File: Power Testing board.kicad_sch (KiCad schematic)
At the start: 13 parts, among them J1 Conn_01x26_Pin, J2 Conn_01x26_Pin, J3 Conn_01x26_Pin, J4 Conn_01x26_Pin, U1 INA260, U2 INA260, U3 INA260, U4 INA260, U5 TPS26631RGE, U6 TPS26631RGE, U7 TPS26631RGE, U8 TPS26631RGE

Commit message: gnd
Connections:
- net GND: now also U1.11 (GND), U1.6 (GND), U2.11 (GND), U2.6 (GND), U3.11 (GND), U3.6 (GND), U4.11 (GND), U4.6 (GND), U5.25 (GND), U5.8 (GND), U6.25 (GND), U6.8 (GND), U7.25 (GND), U7.8 (GND), U8.25 (GND), U8.8 (GND)
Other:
- moved on the sheet: J1, J2, J3, J4

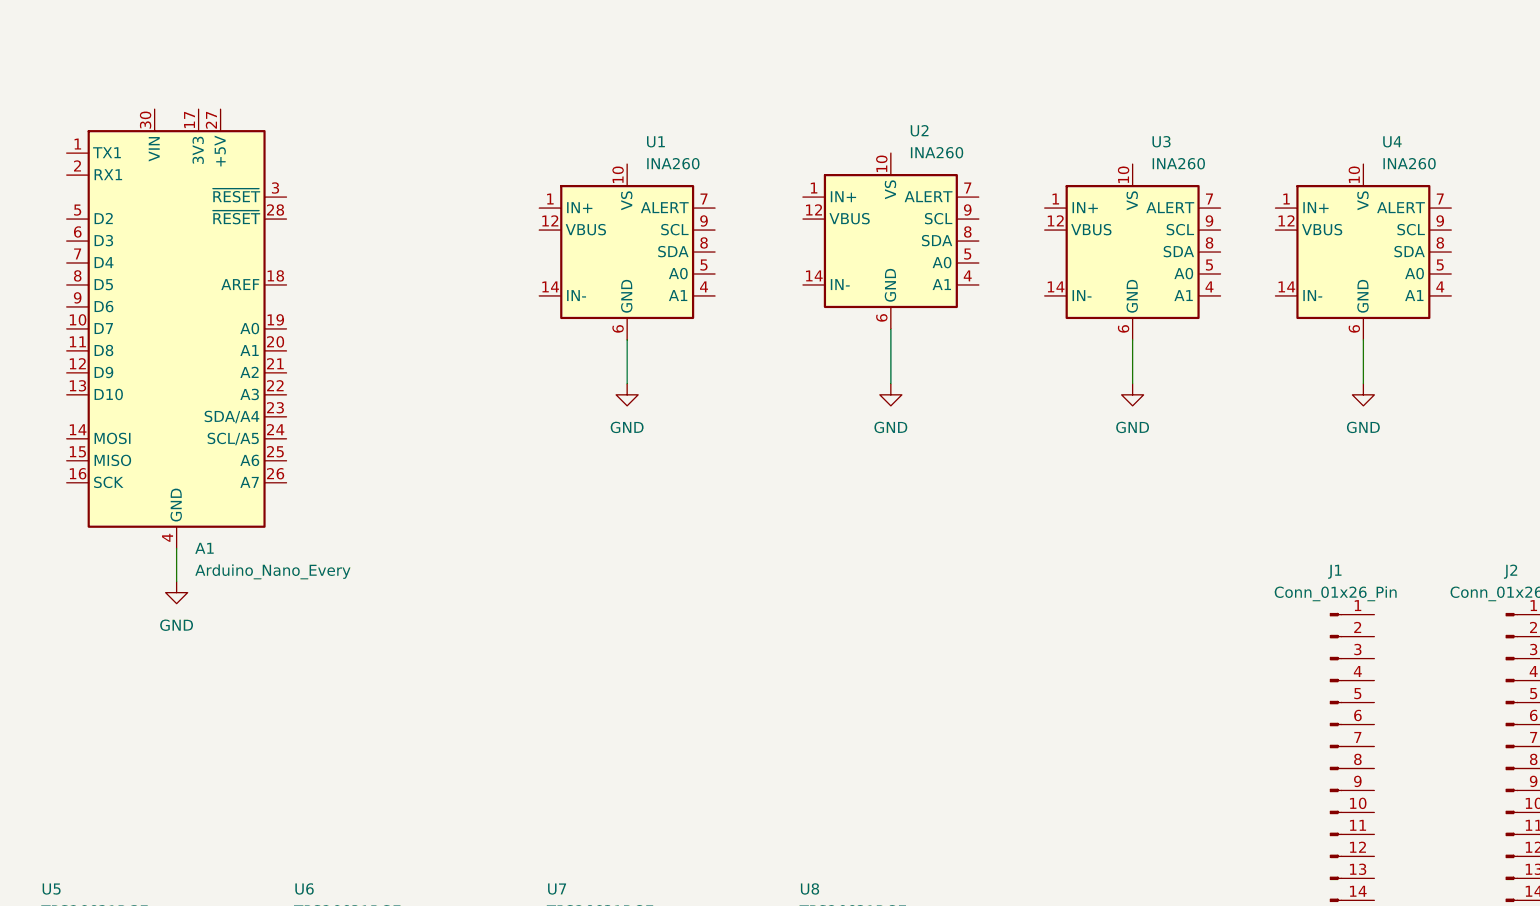
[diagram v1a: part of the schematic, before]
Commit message: ina260 starting connects
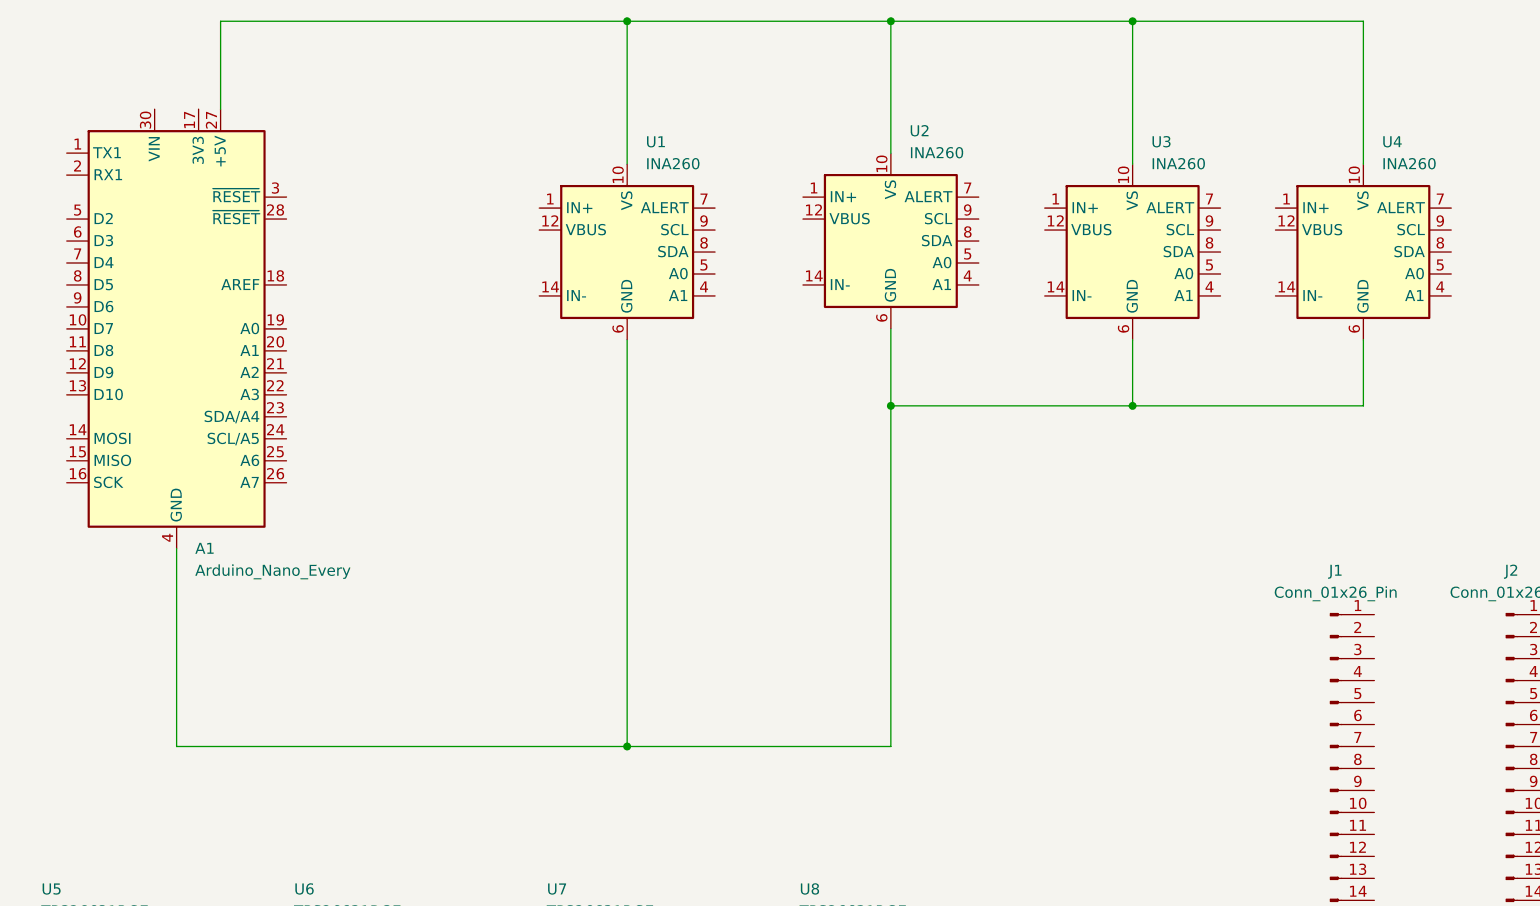
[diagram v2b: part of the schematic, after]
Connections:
- net GND: no longer A1.29 (GND), A1.4 (GND), U1.11 (GND), U1.6 (GND), U2.11 (GND), U2.6 (GND), U3.11 (GND), U3.6 (GND), U4.11 (GND), U4.6 (GND)
- net at U1.10 (VS): now also A1.27 (+5V), U2.10 (VS), U3.10 (VS), U4.10 (VS)
- new net: A1.29 (GND), A1.4 (GND), U1.11 (GND), U1.6 (GND), U2.11 (GND), U2.6 (GND), U3.11 (GND), U3.6 (GND), U4.11 (GND), U4.6 (GND)

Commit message: GN
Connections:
- net GND: now also A1.29 (GND), A1.4 (GND), U1.11 (GND), U1.6 (GND), U2.11 (GND), U2.6 (GND), U3.11 (GND), U3.6 (GND), U4.11 (GND), U4.6 (GND)
- net +3V3_PSU: now reaches U1.1 (IN+), U1.2 (IN+), U1.3 (IN+)
- net +3V3_LOAD: now reaches U1.14 (IN-), U1.15 (IN-), U1.16 (IN-)
- net +5V_PSU: now reaches U2.1 (IN+), U2.2 (IN+), U2.3 (IN+)
- net +5V_LOAD: now reaches U2.14 (IN-), U2.15 (IN-), U2.16 (IN-)
- net +16V8_BOOST: now reaches U4.1 (IN+), U4.2 (IN+), U4.3 (IN+)
- net +16V8_LOAD: now reaches U4.14 (IN-), U4.15 (IN-), U4.16 (IN-)
- net +12V_PSU: now reaches U3.1 (IN+), U3.2 (IN+), U3.3 (IN+)
- net +12V_LOAD: now reaches U3.14 (IN-), U3.15 (IN-), U3.16 (IN-)
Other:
- moved on the sheet: A1, U1, U2, U3, U4

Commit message: i2C
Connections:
- net GND: now also U1.4 (A1), U1.5 (A0), U2.4 (A1), U3.5 (A0)
- net at A1.27 (+5V), U1.10 (VS), U2.10 (VS)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: now also U2.5 (A0), U3.4 (A1), U4.4 (A1), U4.5 (A0)
- net SDA: now reaches U1.8 (SDA)
- net SDA: now also A1.23 (SDA/A4), U2.8 (SDA), U3.8 (SDA), U4.8 (SDA)
- net SCL: now reaches U1.9 (SCL)
- net SCL: now also A1.24 (SCL/A5), U2.9 (SCL), U3.9 (SCL), U4.9 (SCL)
- net +12V_LOAD renamed +12V_MON
- net +16V8_LOAD renamed +16V8_MON
- net +3V3_LOAD renamed +3V3_MON
- net +5V_LOAD renamed +5V_MON
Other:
- moved on the sheet: A1, U2, U3, U4

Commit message: New pages
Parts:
- removed U5, U6, U7, U8: TPS26631RGE, Package_DFN_QFN:Texas_RGE0024H_VQFN-24-1EP_4x4mm_P0.5mm_EP2.7x2.7mm_ThermalVias, symbol Power_Management:TPS26631RGE
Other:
- added sheet Headers (Headers.kicad_sch)
- added sheet Untitled Sheet (untitled.kicad_sch)
- company: (none) -> CSULB SHARKSAT TEAM
- title: (none) -> Power Testing Board

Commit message: page
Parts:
- removed J1, J2, J3, J4: Conn_01x26_Pin, Connector_PinHeader_2.54mm:PinHeader_1x26_P2.54mm_Vertical, symbol Connector:Conn_01x26_Pin

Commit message: GPT progress
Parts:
- removed A1: Arduino_Nano_Every, Module:Arduino_Nano, symbol MCU_Module:Arduino_Nano_Every
- removed U1, U2, U3, U4: INA260, Package_SO:TSSOP-16_4.4x5mm_P0.65mm, symbol Sensor:INA260
- added A1: Arduino Nano USB-powered socket, Module:Arduino_Nano, symbol Power_Testing_Board:Arduino_Nano_USB_Powered
- added C1, C3, C5, C7: 1uF input close to eFuse, Capacitor_SMD:C_0805_2012Metric, symbol Power_Testing_Board:C
- added C2, C4, C6, C8: 10uF output close to eFuse, Capacitor_SMD:C_0805_2012Metric, symbol Power_Testing_Board:C
- added J1: J_ATX_PWR: 3V3 3V3 5V 5V 12V 12V GNDx4, TerminalBlock:TerminalBlock_MaiXu_MX126-5.0-10P_1x10_P5.00mm, symbol Power_Testing_Board:Conn_01x10
- added J2: J_ATX_CTRL: PS_ON PWR_OK 5VSB GND, TerminalBlock:TerminalBlock_MaiXu_MX126-5.0-04P_1x04_P5.00mm, symbol Power_Testing_Board:Conn_01x04
- added J3: ATX_SWITCH, TerminalBlock:TerminalBlock_MaiXu_MX126-5.0-02P_1x02_P5.00mm, symbol Power_Testing_Board:Conn_01x02
- added J4: DEDICATED OUTPUTS: 3V3/G 5V/G 12V/G 16V8/G, TerminalBlock:TerminalBlock_MaiXu_MX126-5.0-08P_1x08_P5.00mm, symbol Power_Testing_Board:Conn_01x08
- added JH1: H1 selected power/GND pins only, Connector_PinSocket_2.54mm:PinSocket_2x26_P2.54mm_Vertical, symbol Power_Testing_Board:PC104_H1_SelectedPowerPins
- added JH2: H2 selected power/GND pins only, Connector_PinSocket_2.54mm:PinSocket_2x26_P2.54mm_Vertical, symbol Power_Testing_Board:PC104_H2_SelectedPowerPins
- added Q1: 2N7002 RESET_3V3 pulldown, Package_TO_SOT_SMD:SOT-23, symbol Power_Testing_Board:NMOS_GSD
- added Q2: 2N7002 RESET_5V pulldown, Package_TO_SOT_SMD:SOT-23, symbol Power_Testing_Board:NMOS_GSD
- added Q3: 2N7002 RESET_12V pulldown, Package_TO_SOT_SMD:SOT-23, symbol Power_Testing_Board:NMOS_GSD
- added Q4: 2N7002 RESET_16V8 pulldown, Package_TO_SOT_SMD:SOT-23, symbol Power_Testing_Board:NMOS_GSD
- added Q5: 2N7002 ATX PS_ON# pulldown, Package_TO_SOT_SMD:SOT-23, symbol Power_Testing_Board:NMOS_GSD
- added R1: 1.10k 1% ILM ~6A, Resistor_SMD:R_0805_2012Metric, symbol Power_Testing_Board:R
- added R10: 249k UVLO top, Resistor_SMD:R_0603_1608Metric, symbol Power_Testing_Board:R
- added R11, R19, R27: 100k UVLO bottom, Resistor_SMD:R_0603_1608Metric, symbol Power_Testing_Board:R
- added R12: 402k OVP top, Resistor_SMD:R_0603_1608Metric, symbol Power_Testing_Board:R
- added R13, R21, R29: 100k OVP bottom, Resistor_SMD:R_0603_1608Metric, symbol Power_Testing_Board:R
- added R14, R22, R30, R33, R6: 330 gate, Resistor_SMD:R_0603_1608Metric, symbol Power_Testing_Board:R
- added R15, R23, R31, R34, R7: 100k gate pulldown, Resistor_SMD:R_0603_1608Metric, symbol Power_Testing_Board:R
- added R16, R24, R32, R8: 10k FLT pullup, Resistor_SMD:R_0603_1608Metric, symbol Power_Testing_Board:R
- added R17, R25, R9: 3.00k 1% ILIM ~6A, Resistor_SMD:R_0805_2012Metric, symbol Power_Testing_Board:R
- added R18: 649k UVLO top, Resistor_SMD:R_0603_1608Metric, symbol Power_Testing_Board:R
- added R2: 100k EN top, Resistor_SMD:R_0603_1608Metric, symbol Power_Testing_Board:R
- added R20: 1.15M OVP top, Resistor_SMD:R_0603_1608Metric, symbol Power_Testing_Board:R
- added R26: 976k UVLO top, Resistor_SMD:R_0603_1608Metric, symbol Power_Testing_Board:R
- added R28: 1.50M OVP top, Resistor_SMD:R_0603_1608Metric, symbol Power_Testing_Board:R
- added R3: 100k EN bottom, Resistor_SMD:R_0603_1608Metric, symbol Power_Testing_Board:R
- added R4: 24.9k OVLO top, Resistor_SMD:R_0603_1608Metric, symbol Power_Testing_Board:R
- added R5: 10k OVLO bottom, Resistor_SMD:R_0603_1608Metric, symbol Power_Testing_Board:R
- added SW1: RESET_3V3 edge button, Button_Switch_THT:SW_PUSH_6mm, symbol Power_Testing_Board:SW_Push
- added SW2: RESET_5V edge button, Button_Switch_THT:SW_PUSH_6mm, symbol Power_Testing_Board:SW_Push
- added SW3: RESET_12V edge button, Button_Switch_THT:SW_PUSH_6mm, symbol Power_Testing_Board:SW_Push
- added SW4: RESET_16V8 edge button, Button_Switch_THT:SW_PUSH_6mm, symbol Power_Testing_Board:SW_Push
- added TP1: +3V3_RAW, TestPoint:TestPoint_Pad_D1.0mm, symbol Power_Testing_Board:TP
- added TP10: +16V8_RAW, TestPoint:TestPoint_Pad_D1.0mm, symbol Power_Testing_Board:TP
- added TP11: +16V8_EFUSE_OUT, TestPoint:TestPoint_Pad_D1.0mm, symbol Power_Testing_Board:TP
- added TP12: +16V8_PROTECTED, TestPoint:TestPoint_Pad_D1.0mm, symbol Power_Testing_Board:TP
- added TP13: GND, TestPoint:TestPoint_Pad_D1.0mm, symbol Power_Testing_Board:TP
- added TP14: I2C_SDA, TestPoint:TestPoint_Pad_D1.0mm, symbol Power_Testing_Board:TP
- added TP15: I2C_SCL, TestPoint:TestPoint_Pad_D1.0mm, symbol Power_Testing_Board:TP
- added TP16: ATX_PS_ON_N, TestPoint:TestPoint_Pad_D1.0mm, symbol Power_Testing_Board:TP
- added TP17: ATX_PWR_OK, TestPoint:TestPoint_Pad_D1.0mm, symbol Power_Testing_Board:TP
- added TP18: +5VSB, TestPoint:TestPoint_Pad_D1.0mm, symbol Power_Testing_Board:TP
- added TP19: RESET_3V3, TestPoint:TestPoint_Pad_D1.0mm, symbol Power_Testing_Board:TP
- added TP2: +3V3_EFUSE_OUT, TestPoint:TestPoint_Pad_D1.0mm, symbol Power_Testing_Board:TP
- added TP20: RESET_5V, TestPoint:TestPoint_Pad_D1.0mm, symbol Power_Testing_Board:TP
- added TP21: RESET_12V, TestPoint:TestPoint_Pad_D1.0mm, symbol Power_Testing_Board:TP
- added TP22: RESET_16V8, TestPoint:TestPoint_Pad_D1.0mm, symbol Power_Testing_Board:TP
- added TP23: FLT_3V3, TestPoint:TestPoint_Pad_D1.0mm, symbol Power_Testing_Board:TP
- added TP24: FLT_5V, TestPoint:TestPoint_Pad_D1.0mm, symbol Power_Testing_Board:TP
- added TP25: FLT_12V, TestPoint:TestPoint_Pad_D1.0mm, symbol Power_Testing_Board:TP
- added TP26: FLT_16V8, TestPoint:TestPoint_Pad_D1.0mm, symbol Power_Testing_Board:TP
- added TP27: BOOST_IN+ (+12V_RAW), TestPoint:TestPoint_Pad_D1.0mm, symbol Power_Testing_Board:TP
- added TP28: BOOST_OUT+ (+16V8_RAW), TestPoint:TestPoint_Pad_D1.0mm, symbol Power_Testing_Board:TP
- added TP29: BOOST_GND, TestPoint:TestPoint_Pad_D1.0mm, symbol Power_Testing_Board:TP
- added TP3: +3V3_PROTECTED, TestPoint:TestPoint_Pad_D1.0mm, symbol Power_Testing_Board:TP
- added TP4: +5V_RAW, TestPoint:TestPoint_Pad_D1.0mm, symbol Power_Testing_Board:TP
- added TP5: +5V_EFUSE_OUT, TestPoint:TestPoint_Pad_D1.0mm, symbol Power_Testing_Board:TP
- added TP6: +5V_PROTECTED, TestPoint:TestPoint_Pad_D1.0mm, symbol Power_Testing_Board:TP
- added TP7: +12V_RAW, TestPoint:TestPoint_Pad_D1.0mm, symbol Power_Testing_Board:TP
- added TP8: +12V_EFUSE_OUT, TestPoint:TestPoint_Pad_D1.0mm, symbol Power_Testing_Board:TP
- added TP9: +12V_PROTECTED, TestPoint:TestPoint_Pad_D1.0mm, symbol Power_Testing_Board:TP
- added U1: TPS259814L 3V3 eFuse latch-off, Package_DFN_QFN:Texas_RPU0010A_VQFN-HR-10_2x2mm_P0.5mm, symbol Power_Testing_Board:TPS259814L_RPW_eFuse
- added U2: TPS26631RGE 5V eFuse, Package_DFN_QFN:Texas_RGE0024H_VQFN-24-1EP_4x4mm_P0.5mm_EP2.7x2.7mm_ThermalVias, symbol Power_Testing_Board:TPS26631RGE_eFuse
- added U3: TPS26631RGE 12V eFuse, Package_DFN_QFN:Texas_RGE0024H_VQFN-24-1EP_4x4mm_P0.5mm_EP2.7x2.7mm_ThermalVias, symbol Power_Testing_Board:TPS26631RGE_eFuse
- added U4: TPS26631RGE 16V8 eFuse, Package_DFN_QFN:Texas_RGE0024H_VQFN-24-1EP_4x4mm_P0.5mm_EP2.7x2.7mm_ThermalVias, symbol Power_Testing_Board:TPS26631RGE_eFuse
- added U5: INA260 3V3 module, Power_Testing_Board:Adafruit_INA260_4226_Module, symbol Power_Testing_Board:Adafruit_INA260_4226_Module
- added U6: INA260 5V module, Power_Testing_Board:Adafruit_INA260_4226_Module, symbol Power_Testing_Board:Adafruit_INA260_4226_Module
- added U7: INA260 12V module, Power_Testing_Board:Adafruit_INA260_4226_Module, symbol Power_Testing_Board:Adafruit_INA260_4226_Module
- added U8: INA260 16V8 module, Power_Testing_Board:Adafruit_INA260_4226_Module, symbol Power_Testing_Board:Adafruit_INA260_4226_Module
- added U9: Boost 12V to 16.8V module 60x42 VERIFIED, Power_Testing_Board:Boost_Module_60x42_VERIFIED, symbol Power_Testing_Board:Boost_Module_60x42
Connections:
- net GND: now also A1.29 (GND), A1.4 (GND), C1.2, C2.2, C3.2, C4.2, C5.2, C6.2, C7.2, C8.2, J1.10 (Pin_10), J1.7 (Pin_7), J1.8 (Pin_8), J1.9 (Pin_9), J2.4 (Pin_4), J3.2 (Pin_2), J4.2 (Pin_2), J4.4 (Pin_4), J4.6 (Pin_6), J4.8 (Pin_8), JH1.22 (H1_22), JH1.24 (H1_24), JH1.27 (H1_27), JH1.31 (H1_31), JH1.32 (H1_32), JH1.36 (H1_36), JH1.39 (H1_39), JH1.40 (H1_40), JH1.42 (H1_42), JH2.29 (H2_29), JH2.30 (H2_30), JH2.31 (H2_31), JH2.32 (H2_32), JH2.36 (H2_36), JH2.39 (H2_39), JH2.40 (H2_40), JH2.41 (H2_41), JH2.42 (H2_42), JH2.43 (H2_43), JH2.44 (H2_44), Q1.2 (S), Q2.2 (S), Q3.2 (S), Q4.2 (S), Q5.2 (S), R1.2, R11.2, R13.2, R15.2, R17.2, R19.2, R21.2, R23.2, R25.2, R27.2, R29.2, R3.2, R31.2, R34.2, R5.2, R7.2, R9.2, SW1.2, SW2.2, SW3.2, SW4.2, TP13.1 (TP), TP29.1 (TP), U1.8 (GND), U2.25 (EP_GND), U2.8 (GND), U3.25 (EP_GND), U3.8 (GND), U4.25 (EP_GND), U4.8 (GND), U5.2 (GND), U6.2 (GND), U7.2 (GND), U8.2 (GND), U9.1 (IN-), U9.3 (OUT-)
- new net +12V_EFUSE_OUT: C6.1, TP8.1 (TP), U3.17 (OUT), U3.18 (OUT), U7.7 (VIN+)
- new net +12V_PROTECTED: J4.5 (Pin_5), JH1.52 (H1_52), TP9.1 (TP), U7.8 (VIN-)
- new net +12V_RAW: C5.1, J1.5 (Pin_5), J1.6 (Pin_6), R18.1, R20.1, TP27.1 (TP), TP7.1 (TP), U3.1 (IN), U3.2 (IN), U3.5 (IN_SYS), U9.2 (IN+)
- new net +16V8_EFUSE_OUT: C8.1, TP11.1 (TP), U4.17 (OUT), U4.18 (OUT), U8.7 (VIN+)
- new net +16V8_PROTECTED: J4.7 (Pin_7), JH2.45 (H2_45), JH2.46 (H2_46), TP12.1 (TP), U8.8 (VIN-)
- new net +16V8_RAW: C7.1, R26.1, R28.1, TP10.1 (TP), TP28.1 (TP), U4.1 (IN), U4.2 (IN), U4.5 (IN_SYS), U9.4 (OUT+)
- new net +3V3_EFUSE_OUT: C2.1, TP2.1 (TP), U1.6 (OUT), U5.7 (VIN+)
- new net +3V3_PROTECTED: J4.1 (Pin_1), JH1.48 (H1_48), JH2.27 (H2_27), JH2.28 (H2_28), TP3.1 (TP), U5.8 (VIN-)
- new net +3V3_RAW: C1.1, J1.1 (Pin_1), J1.2 (Pin_2), R2.1, R4.1, TP1.1 (TP), U1.5 (IN)
- new net +5VSB: J2.3 (Pin_3), TP18.1 (TP)
- new net +5V_EFUSE_OUT: C4.1, TP5.1 (TP), U2.17 (OUT), U2.18 (OUT), U6.7 (VIN+)
- new net +5V_PROTECTED: J4.3 (Pin_3), JH1.47 (H1_47), JH1.49 (H1_49), JH2.25 (H2_25), JH2.26 (H2_26), TP6.1 (TP), U6.8 (VIN-)
- new net +5V_RAW: C3.1, J1.3 (Pin_3), J1.4 (Pin_4), R10.1, R12.1, TP4.1 (TP), U2.1 (IN), U2.2 (IN), U2.5 (IN_SYS)
- new net +ARDUINO_5V: A1.27 (5V), R16.2, R24.2, R32.2, R8.2, U5.1 (VCC), U6.1 (VCC), U7.1 (VCC), U8.1 (VCC)
- new net ALERT_12V: U7.5 (ALERT)
- new net ALERT_16V8: U8.5 (ALERT)
- new net ALERT_3V3: U5.5 (ALERT)
- new net ALERT_5V: U6.5 (ALERT)
- new net ARD_RESET_12V: A1.7 (D4), R22.1
- new net ARD_RESET_16V8: A1.8 (D5), R30.1
- new net ARD_RESET_3V3: A1.5 (D2), R6.1
- new net ARD_RESET_5V: A1.6 (D3), R14.1
- new net ATX_PS_ON_CTL: A1.13 (D10), R33.1
- new net ATX_PS_ON_N: J2.1 (Pin_1), J3.1 (Pin_1), Q5.3 (D), TP16.1 (TP)
- new net ATX_PWR_OK: A1.14 (D11), J2.2 (Pin_2), TP17.1 (TP)
- new net FLT_12V: A1.11 (D8), R24.1, TP25.1 (TP), U3.14 (~FLT)
- new net FLT_16V8: A1.12 (D9), R32.1, TP26.1 (TP), U4.14 (~FLT)
- new net FLT_3V3: A1.9 (D6), R8.1, TP23.1 (TP), U1.4 (~FLT)
- new net FLT_5V: A1.10 (D7), R16.1, TP24.1 (TP), U2.14 (~FLT)
- new net GATE_12V: Q3.1 (G), R22.2, R23.1
- new net GATE_16V8: Q4.1 (G), R30.2, R31.1
- new net GATE_3V3: Q1.1 (G), R6.2, R7.1
- new net GATE_5V: Q2.1 (G), R14.2, R15.1
- new net GATE_PS_ON: Q5.1 (G), R33.2, R34.1
- new net I2C_SCL: A1.24 (A5/SCL), TP15.1 (TP), U5.3 (SCL), U6.3 (SCL), U7.3 (SCL), U8.3 (SCL)
- new net I2C_SDA: A1.23 (A4/SDA), TP14.1 (TP), U5.4 (SDA), U6.4 (SDA), U7.4 (SDA), U8.4 (SDA)
- new net ILIM_12V: R17.1, U3.10 (ILIM)
- new net ILIM_16V8: R25.1, U4.10 (ILIM)
- new net ILIM_3V3: R1.1, U1.9 (ILM)
- new net ILIM_5V: R9.1, U2.10 (ILIM)
- new net IMON_12V: U3.13 (IMON)
- new net IMON_16V8: U4.13 (IMON)
- new net IMON_5V: U2.13 (IMON)
- new net OVLO_3V3: R4.2, R5.1, U1.2 (EN/OVLO)
- new net OVP_12V: R20.2, R21.1, U3.7 (OVP)
- new net OVP_16V8: R28.2, R29.1, U4.7 (OVP)
- new net OVP_5V: R12.2, R13.1, U2.7 (OVP)
- new net PG_12V: U3.16 (PGOOD)
- new net PG_16V8: U4.16 (PGOOD)
- new net PG_3V3: U1.3 (PG)
- new net PG_5V: U2.16 (PGOOD)
- new net RESET_12V: Q3.3 (D), SW3.1, TP21.1 (TP), U3.12 (~SHDN)
- new net RESET_16V8: Q4.3 (D), SW4.1, TP22.1 (TP), U4.12 (~SHDN)
- new net RESET_3V3: Q1.3 (D), R2.2, R3.1, SW1.1, TP19.1 (TP), U1.1 (EN/UVLO)
- new net RESET_5V: Q2.3 (D), SW2.1, TP20.1 (TP), U2.12 (~SHDN)
- new net UVLO_12V: R18.2, R19.1, U3.6 (UVLO)
- new net UVLO_16V8: R26.2, R27.1, U4.6 (UVLO)
- new net UVLO_5V: R10.2, R11.1, U2.6 (UVLO)
- no-connect marks 0 -> 25
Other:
- removed sheet Headers
- removed sheet Untitled Sheet
- note added: "Boost module footprint uses physically verified 60 mm x 42 mm x 20 mm module geometry."
- note added: "Compact layout choice: eFuse ICs are on the main PCB for minimum size. If field replacement becomes more important than area, move each eFuse circuit to a plug-in daughterboard."
- note added: "Only user-selected H1/H2 mission power and GND pins are connected. Excluded/communication pins are not represented in this schematic."
- note added: "Power path on every rail: RAW -> eFuse -> INA260 VIN+ -> INA260 VIN- -> PROTECTED output. INA260 VIN- is the downstream positive rail, never GND."
- title: Power Testing Board -> Compact CubeSat EPS Power Testing Board

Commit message: chat gpt pt.2
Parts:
- C1, C3: value 1uF input close to eFuse -> 1uF 25V X7R input close to eFuse
- C2, C4: value 10uF output close to eFuse -> 10uF 25V X7R output close to eFuse
- C5, C7: value 1uF input close to eFuse -> 1uF 50V X7R input close to eFuse
- C6, C8: value 10uF output close to eFuse -> 10uF 50V X7R output close to eFuse
- R10: value 249k UVLO top -> 261k 1% UVLO top 4.33V
- R11, R19, R27: value 100k UVLO bottom -> 100k 1% UVLO bottom
- R12: value 402k OVP top -> 383k 1% OVP top 5.80V
- R13, R21, R29: value 100k OVP bottom -> 100k 1% OVP bottom
- R18: value 649k UVLO top -> 806k 1% UVLO top 10.87V
- R2: value 100k EN top -> 100k 1% EN top 2.40V
- R20: value 1.15M OVP top -> 1.05M 1% OVP top 13.80V
- R26: value 976k UVLO top -> 1.07M 1% UVLO top 14.04V
- R28: value 1.50M OVP top -> 1.40M 1% OVP top 18.00V
- R3: value 100k EN bottom -> 100k 1% EN bottom
- R4: value 24.9k OVLO top -> 24.9k 1% OVLO top 4.19V
- R5: value 10k OVLO bottom -> 10k 1% OVLO bottom
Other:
- note added: "Serviceable layout choice: eFuse ICs are on the main PCB for manufacturer assembly. If field replacement becomes more important than board area, move each eFuse circuit to a plug-in daughterboard."
- note removed: "Compact layout choice: eFuse ICs are on the main PCB for minimum size. If field replacement becomes more important than area, move each eFuse circuit to a plug-in daughterboard."
